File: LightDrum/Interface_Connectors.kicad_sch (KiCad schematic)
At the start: 2 parts, among them J6 Conn_02x12_Odd_Even, J7 Conn_02x12_Odd_Even

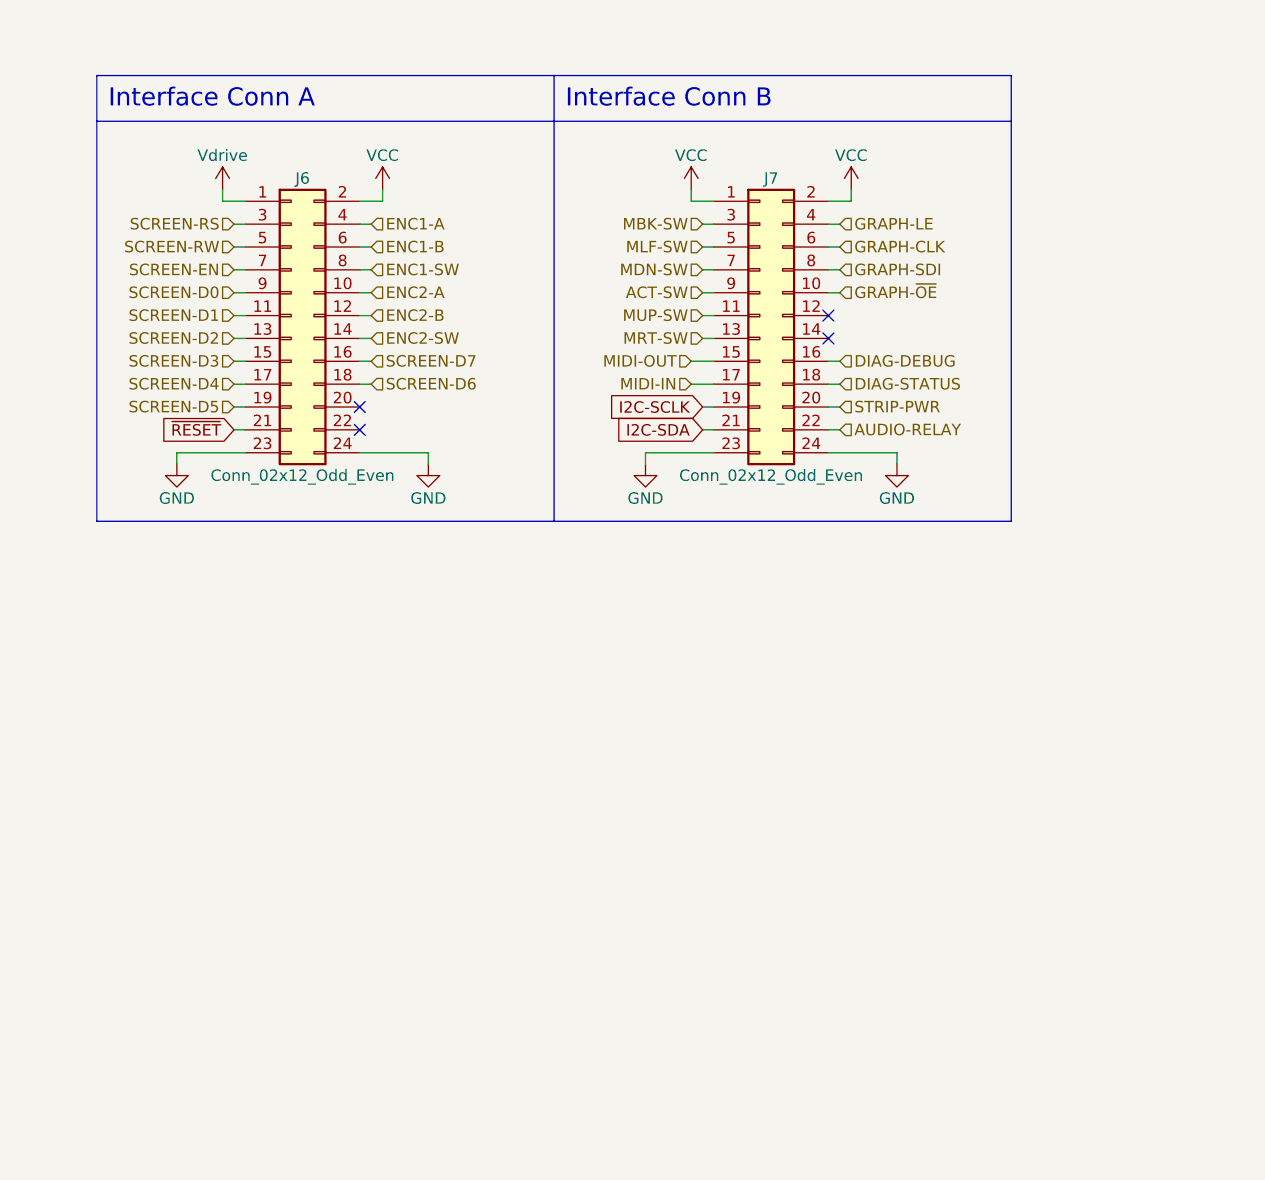
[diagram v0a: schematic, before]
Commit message: Replace interface harnesses with FPC cable
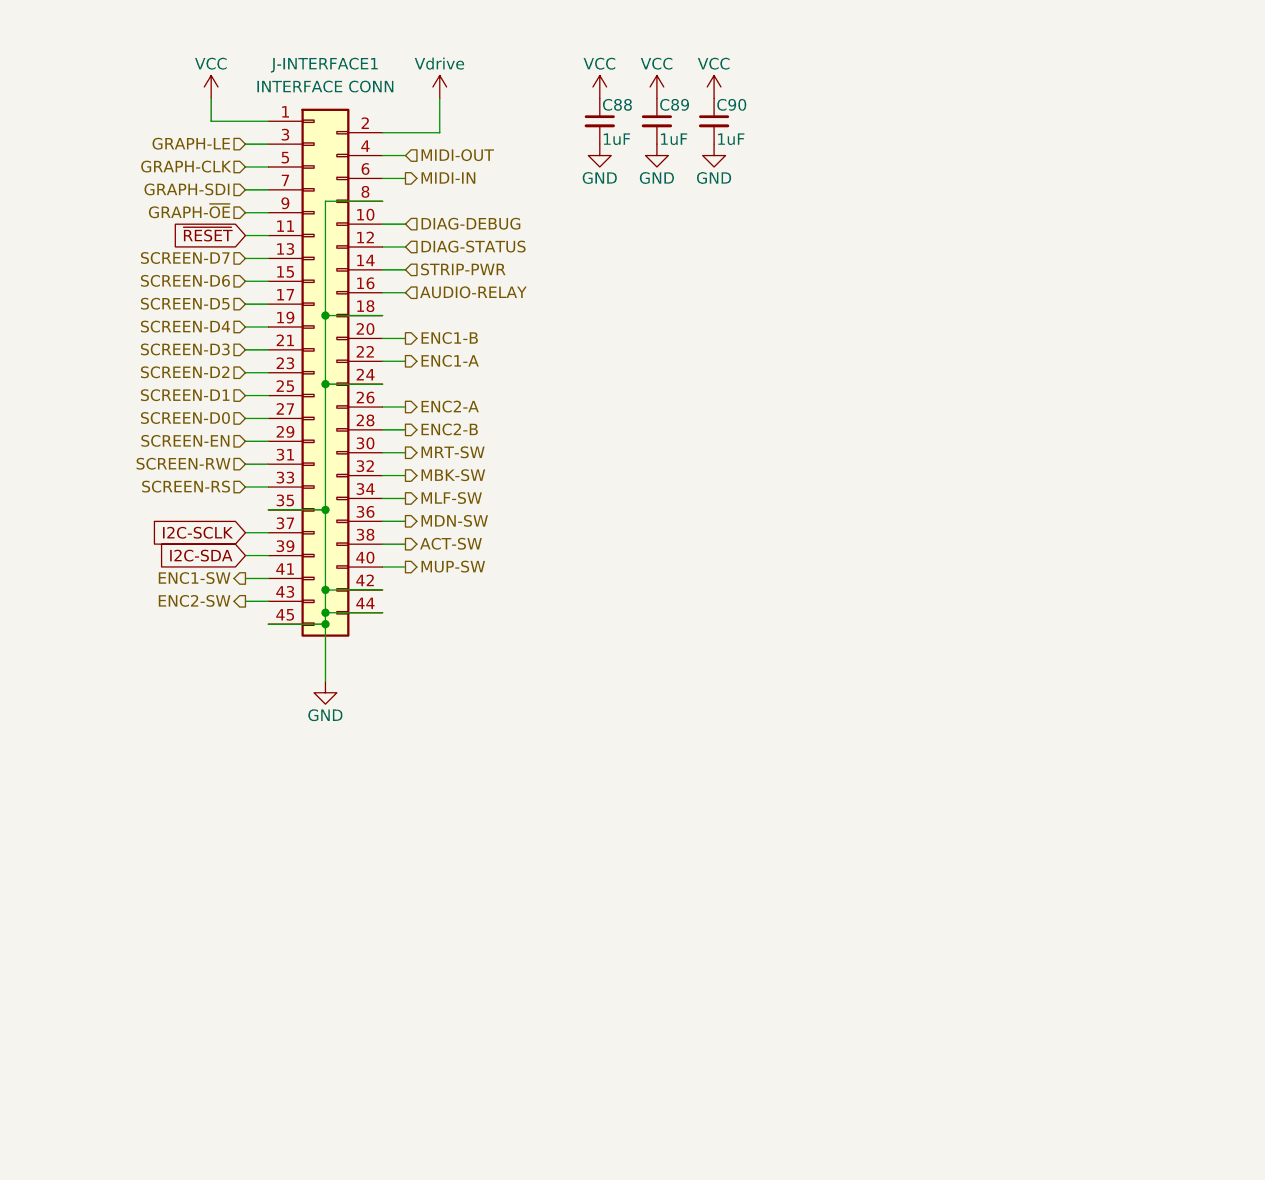
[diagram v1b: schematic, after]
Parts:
- removed J6, J7: Conn_02x12_Odd_Even, Daxxn_Connectors:B24B-PHDSS(LF)(SN), symbol Connector_Generic:Conn_02x12_Odd_Even
- added C88, C89, C90: 1uF, Capacitor_SMD:C_1206_3216Metric, symbol Device:C_Small
- added J-INTERFACE1: INTERFACE CONN, Daxxn_Connectors:046841045100846+, symbol Daxxn_Connectors:Conn_2-45_Odd_Even
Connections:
- net ACT-SW: now also J-INTERFACE1.38 (Pin_38)
- net AUDIO-RELAY: now also J-INTERFACE1.16 (Pin_16)
- net DIAG-DEBUG: now also J-INTERFACE1.10 (Pin_10)
- net DIAG-STATUS: now also J-INTERFACE1.12 (Pin_12)
- net ENC1-A: now also J-INTERFACE1.22 (Pin_22)
- net ENC1-B: now also J-INTERFACE1.20 (Pin_20)
- net ENC1-SW: now also J-INTERFACE1.41 (Pin_41)
- net ENC2-A: now also J-INTERFACE1.26 (Pin_26)
- net ENC2-B: now also J-INTERFACE1.28 (Pin_28)
- net ENC2-SW: now also J-INTERFACE1.43 (Pin_43)
- net GND: now also C88.2, C89.2, C90.2, J-INTERFACE1.18 (Pin_18), J-INTERFACE1.24 (Pin_24), J-INTERFACE1.35 (Pin_35), J-INTERFACE1.42 (Pin_42), J-INTERFACE1.44 (Pin_44), J-INTERFACE1.45 (Pin_45), J-INTERFACE1.8 (Pin_8)
- net GRAPH-CLK: now also J-INTERFACE1.5 (Pin_5)
- net GRAPH-LE: now also J-INTERFACE1.3 (Pin_3)
- net GRAPH-SDI: now also J-INTERFACE1.7 (Pin_7)
- net GRAPH-~{OE}: now also J-INTERFACE1.9 (Pin_9)
- net I2C-SCLK: now also J-INTERFACE1.37 (Pin_37)
- net I2C-SDA: now also J-INTERFACE1.39 (Pin_39)
- net MBK-SW: now also J-INTERFACE1.32 (Pin_32)
- net MDN-SW: now also J-INTERFACE1.36 (Pin_36)
- net MIDI-IN: now also J-INTERFACE1.6 (Pin_6)
- net MIDI-OUT: now also J-INTERFACE1.4 (Pin_4)
- net MLF-SW: now also J-INTERFACE1.34 (Pin_34)
- net MRT-SW: now also J-INTERFACE1.30 (Pin_30)
- net MUP-SW: now also J-INTERFACE1.40 (Pin_40)
- net SCREEN-D0: now also J-INTERFACE1.27 (Pin_27)
- net SCREEN-D1: now also J-INTERFACE1.25 (Pin_25)
- net SCREEN-D2: now also J-INTERFACE1.23 (Pin_23)
- net SCREEN-D3: now also J-INTERFACE1.21 (Pin_21)
- net SCREEN-D4: now also J-INTERFACE1.19 (Pin_19)
- net SCREEN-D5: now also J-INTERFACE1.17 (Pin_17)
- net SCREEN-D6: now also J-INTERFACE1.15 (Pin_15)
- net SCREEN-D7: now also J-INTERFACE1.13 (Pin_13)
- net SCREEN-EN: now also J-INTERFACE1.29 (Pin_29)
- net SCREEN-RS: now also J-INTERFACE1.33 (Pin_33)
- net SCREEN-RW: now also J-INTERFACE1.31 (Pin_31)
- net STRIP-PWR: now also J-INTERFACE1.14 (Pin_14)
- net VCC: now also C88.1, C89.1, C90.1, J-INTERFACE1.1 (Pin_1)
- net Vdrive: now also J-INTERFACE1.2 (Pin_2)
- net ~{RESET}: now also J-INTERFACE1.11 (Pin_11)
- no-connect marks 4 -> 0
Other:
- note removed: "Interface Conn A"
- note removed: "Interface Conn B"

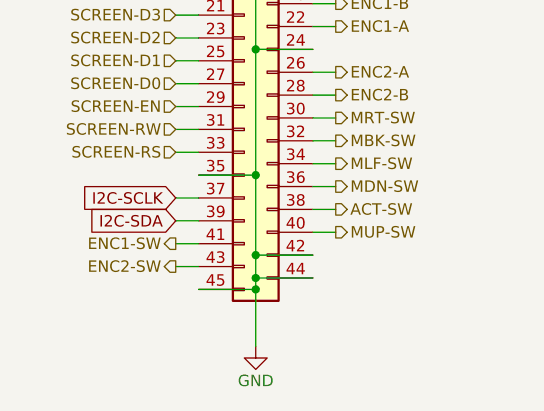
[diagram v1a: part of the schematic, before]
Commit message: Add extra vcc pin to FPC conn
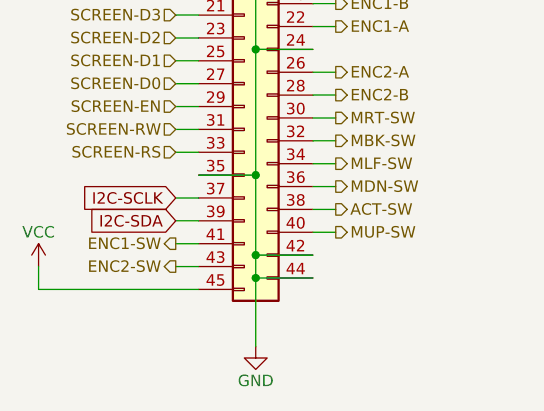
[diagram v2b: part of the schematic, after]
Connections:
- net GND: no longer J-INTERFACE1.45 (Pin_45)
- net VCC: now also J-INTERFACE1.45 (Pin_45)
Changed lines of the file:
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@@
   (junction (at 50.8 55.88) (diameter 0) (color 0 0 0 0)
   )
-  (junction (at 50.8 82.55) (diameter 0) (color 0 0 0 0)
-  )
   (wire (pts (xy 63.5 27.94) (xy 63.5 24.13))
     (stroke (width 0) (type default) (color 0 0 0 0))
@@
     (stroke (width 0) (type default) (color 0 0 0 0))
   )
-  (wire (pts (xy 50.8 81.28) (xy 50.8 82.55))
+  (wire (pts (xy 50.8 81.28) (xy 50.8 88.9))
     (stroke (width 0) (type default) (color 0 0 0 0))
   )
@@
     (stroke (width 0) (type default) (color 0 0 0 0))
   )
+  (wire (pts (xy 26.67 80.01) (xy 26.67 82.55))
+    (stroke (width 0) (type default) (color 0 0 0 0))
+  )
   (wire (pts (xy 57.15 66.04) (xy 59.69 66.04))
     (stroke (width 0) (type default) (color 0 0 0 0))
@@
     (stroke (width 0) (type default) (color 0 0 0 0))
   )
-  (wire (pts (xy 50.8 82.55) (xy 50.8 88.9))
-    (stroke (width 0) (type default) (color 0 0 0 0))
-  )
   (wire (pts (xy 41.91 44.45) (xy 44.45 44.45))
     (stroke (width 0) (type default) (color 0 0 0 0))
@@
     (stroke (width 0) (type default) (color 0 0 0 0))
   )
-  (wire (pts (xy 44.45 82.55) (xy 50.8 82.55))
-    (stroke (width 0) (type default) (color 0 0 0 0))
-  )
   (wire (pts (xy 41.91 41.91) (xy 44.45 41.91))
     (stroke (width 0) (type default) (color 0 0 0 0))
@@
   )
   (wire (pts (xy 41.91 59.69) (xy 44.45 59.69))
+    (stroke (width 0) (type default) (color 0 0 0 0))
+  )
+  (wire (pts (xy 44.45 82.55) (xy 26.67 82.55))
     (stroke (width 0) (type default) (color 0 0 0 0))
   )
@@
       (effects (font (size 1.27 1.27)) hide)
     )
+    (pin "1")
+  )
+  (symbol (lib_id "power:VCC") (at 26.67 80.01 0) (unit 1)
+    (in_bom yes) (on_board yes)
+    (property "Reference" "#PWR0132" (id 0) (at 26.67 83.82 0)
+      (effects (font (size 1.27 1.27)) hide)
+    )
+    (property "Value" "VCC" (id 1) (at 26.67 76.2 0))
+    (property "Footprint" "" (id 2) (at 26.67 80.01 0)
+      (effects (font (size 1.27 1.27)) hide)
+    )
+    (property "Datasheet" "" (id 3) (at 26.67 80.01 0)
+      (effects (font (size 1.27 1.27)) hide)
+    )

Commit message: Add docs and gerbers for REV7
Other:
- title: (none) -> LightDrum
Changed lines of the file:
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@@
   (paper "A4")
   (title_block
-    (rev "REV6")
+    (title "LightDrum")
+    (rev "REV7")
     (company "Daxxn Industries")
   )

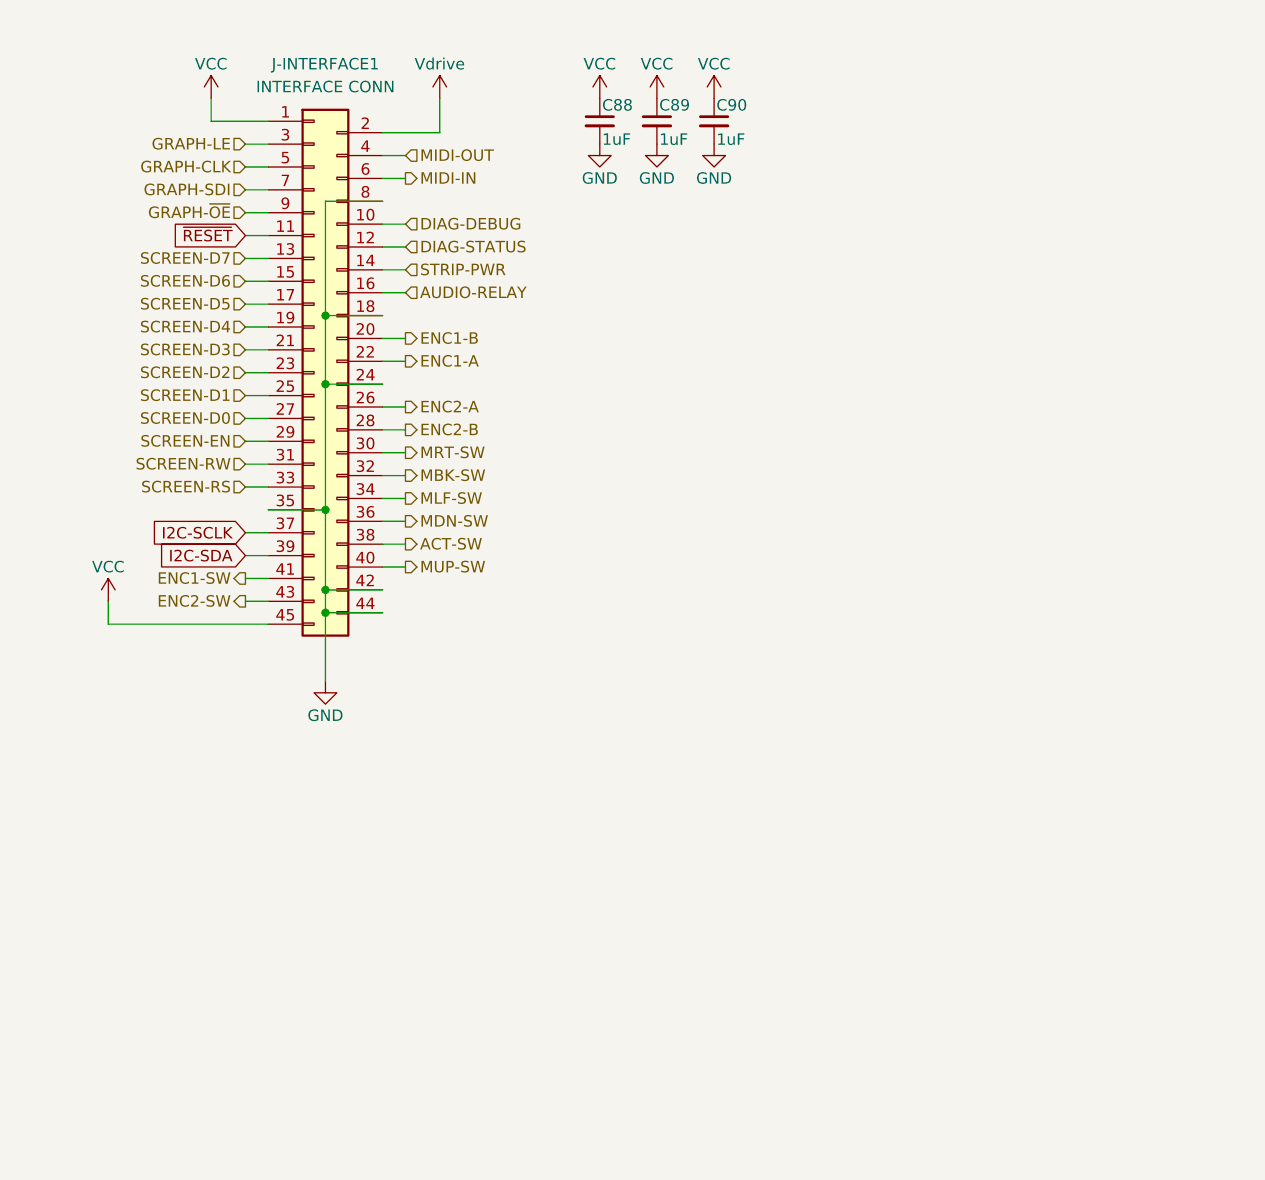
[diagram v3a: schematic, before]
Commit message: Replace screen (WIP)
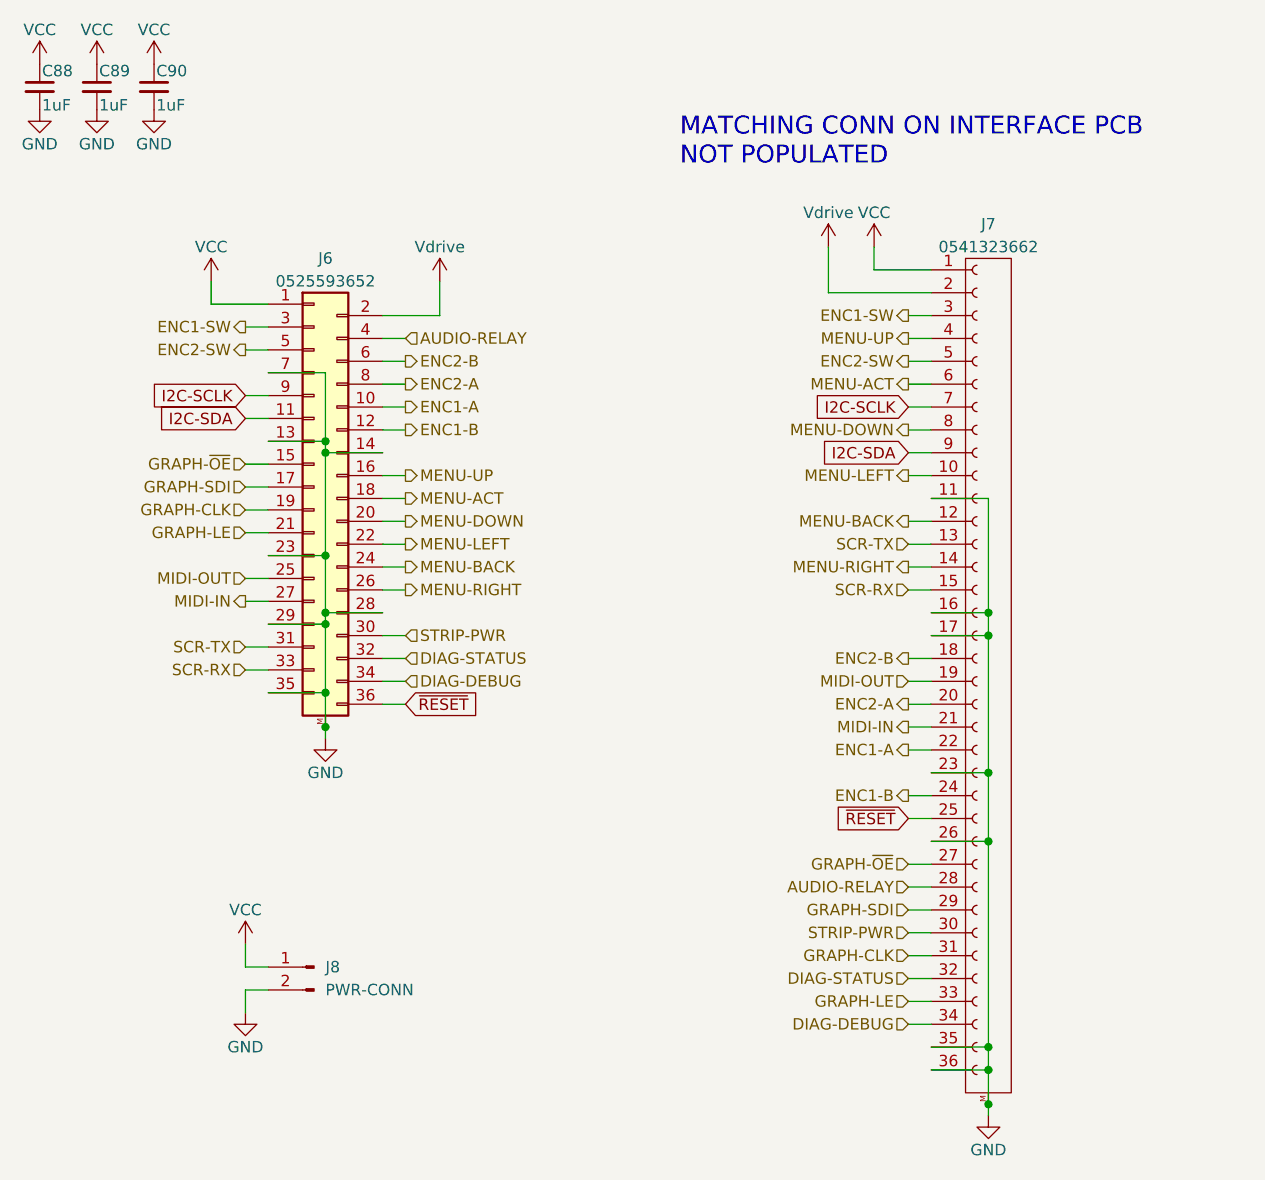
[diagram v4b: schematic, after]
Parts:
- removed J-INTERFACE1: INTERFACE CONN, Daxxn_Connectors:046841045100846+, symbol Daxxn_Connectors:Conn_2-45_Odd_Even
- added J6: 0525593652, Daxxn_Connectors:0525593652, symbol Daxxn_Connectors:0525593652
- added J7: 0541323662, Daxxn_Connectors:0541323662, symbol Daxxn_Connectors:0541323662
- added J8: PWR-CONN, Connector_JST:JST_XA_B02B-XASK-1_1x02_P2.50mm_Vertical, symbol Connector:Conn_01x02_Male
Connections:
- net AUDIO-RELAY: now also J6.4 (Pin_4), J7.28 (Pin_28)
- net DIAG-DEBUG: now also J6.34 (Pin_34), J7.34 (Pin_34)
- net DIAG-STATUS: now also J6.32 (Pin_32), J7.32 (Pin_32)
- net ENC1-A: now also J6.10 (Pin_10), J7.22 (Pin_22)
- net ENC1-B: now also J6.12 (Pin_12), J7.24 (Pin_24)
- net ENC1-SW: now also J6.3 (Pin_3), J7.3 (Pin_3)
- net ENC2-A: now also J6.8 (Pin_8), J7.20 (Pin_20)
- net ENC2-B: now also J6.6 (Pin_6), J7.18 (Pin_18)
- net ENC2-SW: now also J6.5 (Pin_5), J7.5 (Pin_5)
- net GND: now also J6.13 (Pin_13), J6.14 (Pin_14), J6.23 (Pin_23), J6.28 (Pin_28), J6.29 (Pin_29), J6.35 (Pin_35), J6.7 (Pin_7), J6.M (MNT), J7.11 (Pin_11), J7.16 (Pin_16), J7.17 (Pin_17), J7.23 (Pin_23), J7.26 (Pin_26), J7.35 (Pin_35), J7.36 (Pin_36), J7.M (MNT), J8.2 (Pin_2)
- net GRAPH-CLK: now also J6.19 (Pin_19), J7.31 (Pin_31)
- net GRAPH-LE: now also J6.21 (Pin_21), J7.33 (Pin_33)
- net GRAPH-SDI: now also J6.17 (Pin_17), J7.29 (Pin_29)
- net GRAPH-~{OE}: now also J6.15 (Pin_15), J7.27 (Pin_27)
- net I2C-SCLK: now also J6.9 (Pin_9), J7.7 (Pin_7)
- net I2C-SDA: now also J6.11 (Pin_11), J7.9 (Pin_9)
- net MIDI-IN: now also J6.27 (Pin_27), J7.21 (Pin_21)
- net MIDI-OUT: now also J6.25 (Pin_25), J7.19 (Pin_19)
- net STRIP-PWR: now also J6.30 (Pin_30), J7.30 (Pin_30)
- net VCC: now also J6.1 (Pin_1), J7.1 (Pin_1), J8.1 (Pin_1)
- net Vdrive: now also J6.2 (Pin_2), J7.2 (Pin_2)
- net ~{RESET}: now also J6.36 (Pin_36), J7.25 (Pin_25)
- new net MENU-ACT: J6.18 (Pin_18), J7.6 (Pin_6)
- new net MENU-BACK: J6.24 (Pin_24), J7.12 (Pin_12)
- new net MENU-DOWN: J6.20 (Pin_20), J7.8 (Pin_8)
- new net MENU-LEFT: J6.22 (Pin_22), J7.10 (Pin_10)
- new net MENU-RIGHT: J6.26 (Pin_26), J7.14 (Pin_14)
- new net MENU-UP: J6.16 (Pin_16), J7.4 (Pin_4)
- new net SCR-RX: J6.33 (Pin_33), J7.15 (Pin_15)
- new net SCR-TX: J6.31 (Pin_31), J7.13 (Pin_13)
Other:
- note added: "MATCHING CONN ON INTERFACE PCB NOT POPULATED"
- moved on the sheet: C88, C89, C90
